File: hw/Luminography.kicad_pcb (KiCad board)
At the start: 2 copper layers, 100 x 100 mm, 112 parts, among them J1 USB_C_Receptacle_PowerOnly_6P, J2 Conn_01x04, Q1 2N7002, SW1 SW_Push, SW2 SW_Push, U1 LTC4054ES5-4.2, U10 MAX98357AETE+, U100 BH1750FVI-TR, U101 BH1750FVI-TR, U102 BH1750FVI-TR, U103 BH1750FVI-TR, U104 BH1750FVI-TR, U105 BH1750FVI-TR, U106 BH1750FVI-TR, U107 BH1750FVI-TR, U108 BH1750FVI-TR, U109 BH1750FVI-TR, U110 BH1750FVI-TR, U111 BH1750FVI-TR, U112 BH1750FVI-TR, U113 BH1750FVI-TR, U114 BH1750FVI-TR, U115 BH1750FVI-TR, U116 BH1750FVI-TR, U117 BH1750FVI-TR, U118 BH1750FVI-TR, U119 BH1750FVI-TR, U120 BH1750FVI-TR, U121 BH1750FVI-TR, U122 BH1750FVI-TR, U123 BH1750FVI-TR, U2 XS3A1T3157GMX, U3 SPX3819M5-L-3-3, U4 MAX17048G+T10, U5 STM32G030K6Tx, U6 ZJY128R-IG01, U7 W25Q16JVUXIQ, U8 BMI270, U9 MMC5603NJ, X1 12.288MHz

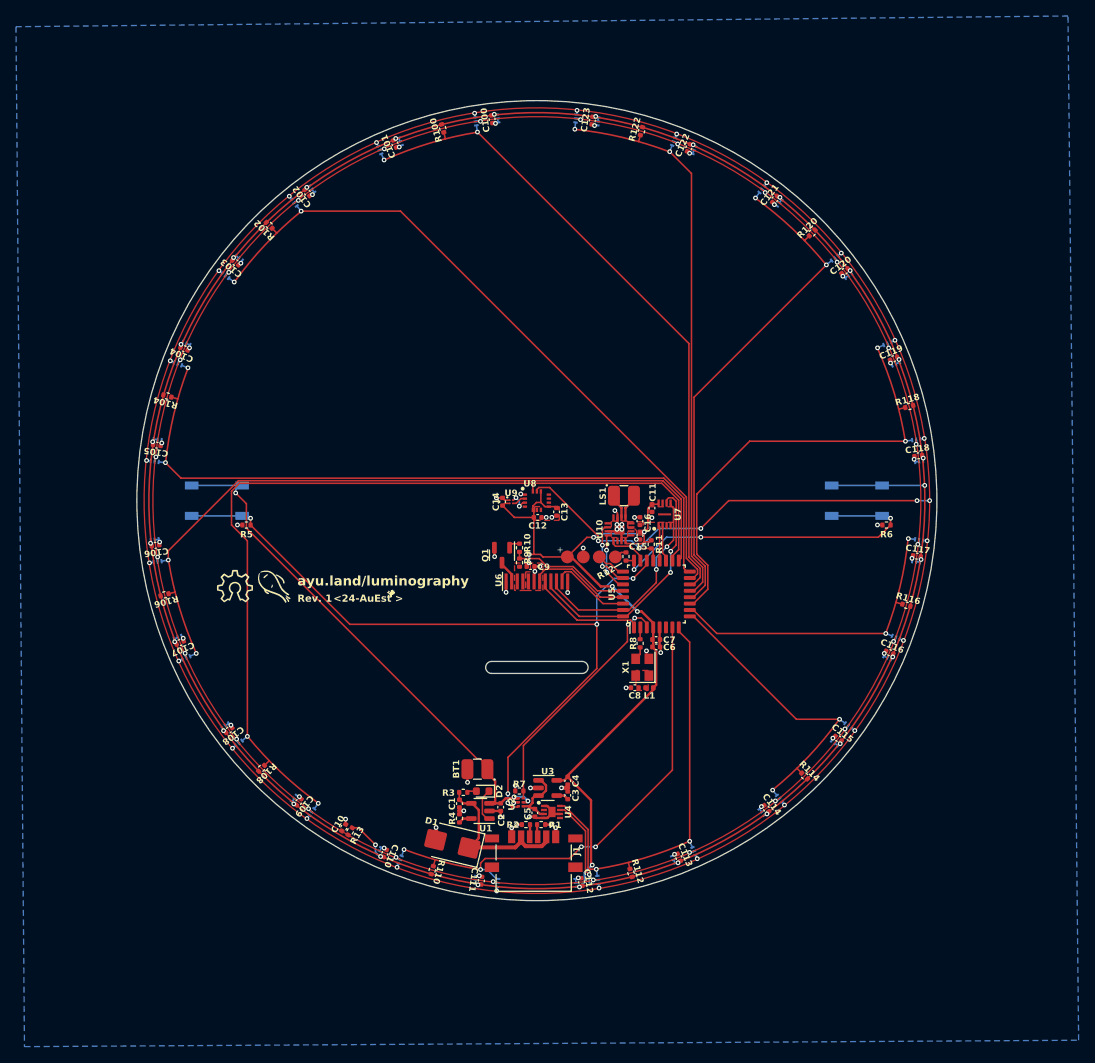
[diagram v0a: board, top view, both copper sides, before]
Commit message: 🚧 Add LEDs
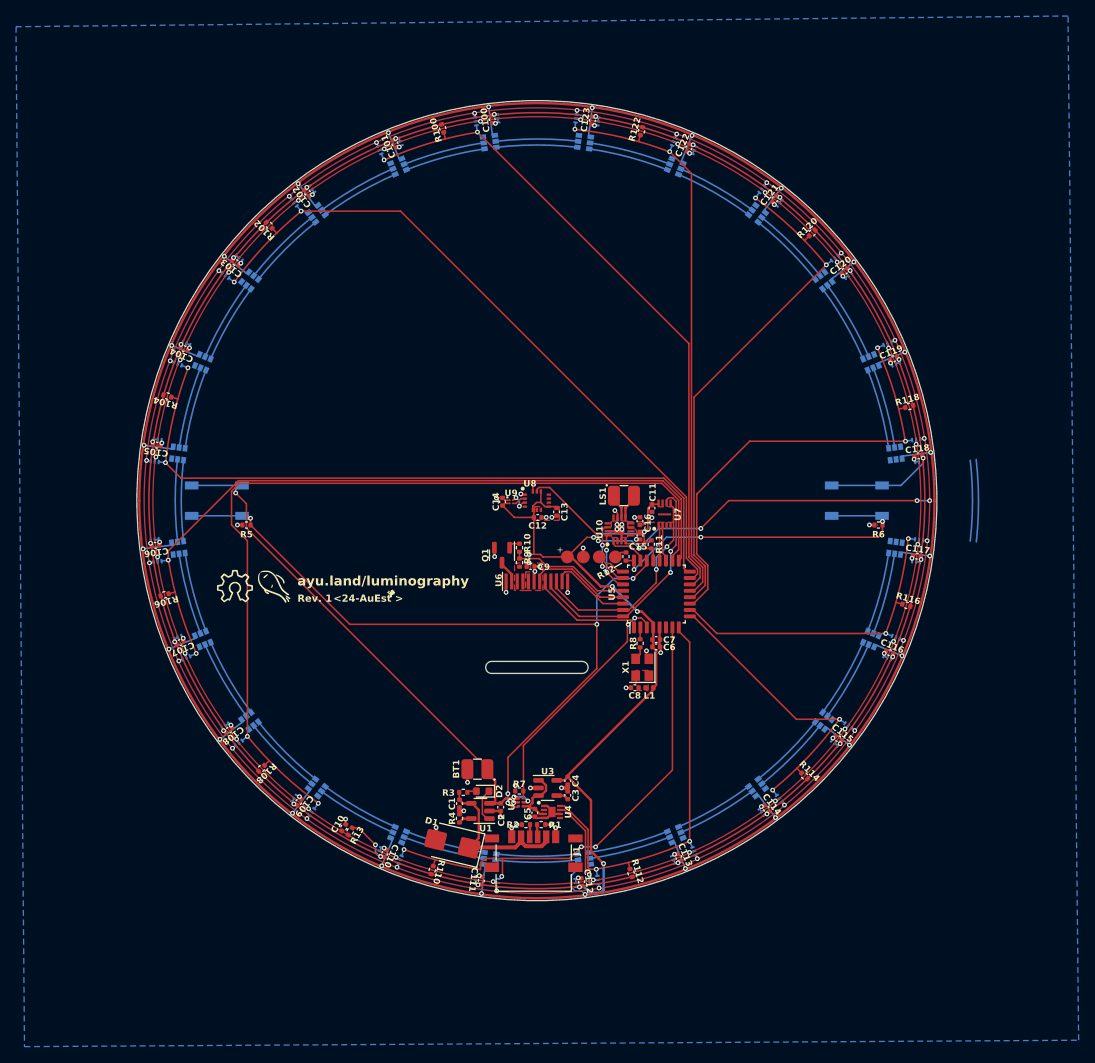
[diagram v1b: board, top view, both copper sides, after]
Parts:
- added U200: HD107S, Luminography_footprints:HD107S_2020_6, B.Cu at (94.1, 55.2)
- added U201: HD107S, Luminography_footprints:HD107S_2020_6, B.Cu at (82.7, 58.2)
- added U202: HD107S, Luminography_footprints:HD107S_2020_6, B.Cu at (72.5, 64.1)
- added U203: HD107S, Luminography_footprints:HD107S_2020_6, B.Cu at (64.1, 72.5)
- added U204: HD107S, Luminography_footprints:HD107S_2020_6, B.Cu at (58.2, 82.7)
- added U205: HD107S, Luminography_footprints:HD107S_2020_6, B.Cu at (55.2, 94.1)
- added U206: HD107S, Luminography_footprints:HD107S_2020_6, B.Cu at (55.2, 105.9)
- added U207: HD107S, Luminography_footprints:HD107S_2020_6, B.Cu at (58.2, 117.3)
- added U208: HD107S, Luminography_footprints:HD107S_2020_6, B.Cu at (64.1, 127.5)
- added U209: HD107S, Luminography_footprints:HD107S_2020_6, B.Cu at (72.5, 135.9)
- added U210: HD107S, Luminography_footprints:HD107S_2020_6, B.Cu at (82.7, 141.8)
- added U211: HD107S, Luminography_footprints:HD107S_2020_6, B.Cu at (94.1, 144.8)
- added U212: HD107S, Luminography_footprints:HD107S_2020_6, B.Cu at (105.9, 144.8)
- added U213: HD107S, Luminography_footprints:HD107S_2020_6, B.Cu at (117.3, 141.8)
- added U214: HD107S, Luminography_footprints:HD107S_2020_6, B.Cu at (127.5, 135.9)
- added U215: HD107S, Luminography_footprints:HD107S_2020_6, B.Cu at (135.9, 127.5)
- added U216: HD107S, Luminography_footprints:HD107S_2020_6, B.Cu at (141.8, 117.3)
- added U217: HD107S, Luminography_footprints:HD107S_2020_6, B.Cu at (144.8, 105.9)
- added U218: HD107S, Luminography_footprints:HD107S_2020_6, B.Cu at (144.8, 94.1)
- added U219: HD107S, Luminography_footprints:HD107S_2020_6, B.Cu at (141.8, 82.7)
- added U220: HD107S, Luminography_footprints:HD107S_2020_6, B.Cu at (135.9, 72.5)
- added U221: HD107S, Luminography_footprints:HD107S_2020_6, B.Cu at (127.5, 64.1)
- added U222: HD107S, Luminography_footprints:HD107S_2020_6, B.Cu at (117.3, 58.2)
- added U223: HD107S, Luminography_footprints:HD107S_2020_6, B.Cu at (105.9, 55.2)
- moved R6 1.00 mm to (142.7, 103.0)
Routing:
- net +5V: track 0.00 -> 370.2 mm, vias 0 -> 24
- net (no net): track 0.00 -> 20.5 mm
- net Net-(U207-CI): track 0.00 -> 10.3 mm
- net Net-(U201-CI): track 0.00 -> 10.3 mm
- net Net-(U216-CI): track 0.00 -> 10.3 mm
- net Net-(U215-CI): track 0.00 -> 10.3 mm
- net Net-(U209-CI): track 0.00 -> 10.3 mm
- net Net-(U204-CI): track 0.00 -> 10.3 mm
- net Net-(U200-CO): track 0.00 -> 10.3 mm
- net Net-(U202-CI): track 0.00 -> 10.3 mm
- net Net-(U222-CI): track 0.00 -> 10.3 mm
- net Net-(U219-CI): track 0.00 -> 10.3 mm
- net Net-(U213-CI): track 0.00 -> 10.3 mm
- net Net-(U221-CI): track 0.00 -> 10.3 mm
- net Net-(U206-CI): track 0.00 -> 10.3 mm
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
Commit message: 🚧 Finally, add LEDS (board revision WIP)
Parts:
- removed the C8 at (112.2, 123.4)
- removed the R12 at (111.1, 107.0)
- removed X1: 12.288MHz, Oscillator:Oscillator_SMD_Abracon_ASE-4Pin_3.2x2.5mm
- added C10: 100n, Capacitor_SMD:C_0402_1005Metric, F.Cu at (116.7, 117.8)
- added C11: 6.8p, Capacitor_SMD:C_0402_1005Metric, F.Cu at (113.0, 121.0)
- added C12: 6.8p, Capacitor_SMD:C_0402_1005Metric, F.Cu at (118.2, 120.7)
- added C14: 100n, Capacitor_SMD:C_0402_1005Metric, F.Cu at (127.5, 106.1)
- added C15: 100n, Capacitor_SMD:C_0402_1005Metric, F.Cu at (128.4, 112.6)
- added C5: 10u, Capacitor_SMD:C_0402_1005Metric, F.Cu at (102.9, 131.8)
- added C6: 10u, Capacitor_SMD:C_0402_1005Metric, F.Cu at (103.2, 127.9)
- added R14: 1M, Resistor_SMD:R_0402_1005Metric, F.Cu at (126.6, 112.6)
- added R9: 2.2k, Resistor_SMD:R_0402_1005Metric, F.Cu at (105.7, 129.3)
- added U4: TPS61220DCK, Package_TO_SOT_SMD:Texas_R-PDSO-G6, F.Cu at (103.4, 129.8)
- added U8: TXS0102DCT, Package_SO:SSOP-8_2.95x2.8mm_P0.65mm, F.Cu at (127.5, 109.4)
- added Y1: 32MHz 12pF, Crystal:Crystal_SMD_3225-4Pin_3.2x2.5mm, F.Cu at (115.6, 121.0)
- L1: value 10n -> 10u; footprint Inductor_SMD:L_0402_1005Metric -> Inductor_SMD:L_Sunlord_SWPA252012S
- R8: value 0 TBD -> 1.8M
- U6: renamed from U5; value STM32G030K6Tx -> STM32G030C8Tx; footprint Package_QFP:LQFP-32_7x7mm_P0.8mm -> Package_QFP:LQFP-48_7x7mm_P0.5mm
- moved L1 15.8 mm to (100.2, 130.9), turned to 90 degrees
- moved R8 13.0 mm to (106.7, 129.3), turned to -90 degrees
- moved C8 0.37 mm to (114.5, 118.3)
- moved C9 0.37 mm to (114.5, 117.4)
- renumbered C9 to C13, C10 to C16, C11 to C17, C12 to C18, C13 to C19, C14 to C20, C15 to C21, C16 to C22, C5 to C7, C6 to C8, C7 to C9, R9 to R10, R10 to R11, R11 to R12, U9 to U10, U8 to U11, U10 to U12, U4 to U5, U6 to U7, U7 to U9
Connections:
- L1 pad 1: VDD -> VRI
- R8 pad 1: Net-(X1-OUT) -> +5V
- R8 pad 2: Net-(U5-PC14) -> Net-(U4-FB)
- U217 pad 5: LED_CLK -> LED_CLK_5V
- U217 pad 6: LED_DATA -> LED_DATA_5V
- U6 pad 1: LCD_CS -> BTNA_INTR
- U6 pad 10: I2Cx_SDA_08 -> Net-(U6-NRST)
- U6 pad 11: I2Cx_SDA_09 -> I2Cx_SDA_05
- U6 pad 12: I2Cx_SDA_10 -> I2Cx_SDA_06
- U6 pad 13: I2Cx_SDA_11 -> I2Cx_SDA_07
- U6 pad 14: I2Cx_SDA_00 -> I2Cx_SDA_08
- U6 pad 15: I2Cx_SDA_01 -> LSH_OE
- U6 pad 16: I2Cx_SDA_02 -> LED_CLK
- U6 pad 17: I2Cx_SDA_03 -> BTNB_INTR
- U6 pad 18: I2Cx_SDA_04 -> LED_DATA
- U6 pad 19: SPI_MISO -> I2Cx_SDA_09
- U6 pad 2: Net-(U5-PC14) -> PWR_LATCH
- U6 pad 20: FLASH_CS -> I2Cx_SDA_10
- U6 pad 21: I2Cx_SCL -> I2Cx_SDA_11
- U6 pad 22: BTNA_INTR -> I2Cx_SDA_00
- U6 pad 23: I2S_SD -> I2Cx_SDA_01
- U6 pad 24: BTNB_INTR -> I2Cx_SDA_02
- U6 pad 25: SWCLK -> I2Cx_SDA_03
- U6 pad 26: I2S_WS -> I2Cx_SDA_04
- U6 pad 27: I2S_CK -> unconnected-(U6-PB15-Pad27)
- U6 pad 28: LCD_BL -> unconnected-(U6-PA8-Pad28)
- U6 pad 29: LCD_DC -> SPI_MISO
- U6 pad 3: PWR_LATCH -> unconnected-(U6-PC15-Pad3)
- U6 pad 30: LCD_RSTN -> FLASH_CS
- U6 pad 31: SPI_MOSI -> unconnected-(U6-PC7-Pad31)
- U6 pad 32: SPI_SCK -> I2Cx_SCL
- U6 pad 5: GND -> VDD
- U6 pad 6: unconnected-(U5-NRST-Pad6) -> VDD
- U6 pad 7: I2Cx_SDA_05 -> GND
- U6 pad 8: I2Cx_SDA_06 -> Net-(U6-PF0)
- U6 pad 9: I2Cx_SDA_07 -> Net-(U6-PF1)
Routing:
- net +5V: track 370.2 -> 404.5 mm, vias 24 -> 26
- net (no net): track 20.5 -> 0.00 mm
- net VDD: track 402.2 -> 420.5 mm, vias 32 -> 33
- net VRI: track 8.10 -> 18.9 mm
- net LSH_OE: track 0.00 -> 9.91 mm
- net LED_DATA: track 0.00 -> 9.55 mm
- net GND: track 48.1 -> 57.1 mm, vias 61 -> 68
- net LED_CLK: track 0.00 -> 8.86 mm
- net BTNB_INTR: track 43.5 -> 35.5 mm, vias 3 -> 1
- net Net-(U6-PF0): track 0.00 -> 8.06 mm
- net Net-(U6-PF1): track 0.00 -> 6.05 mm
- net BTNA_INTR: track 97.2 -> 93.4 mm, vias 5 -> 3
- net PWR_LATCH: track 30.6 -> 27.8 mm, vias 2 -> 0
- net Net-(U4-FB): track 0.00 -> 2.25 mm
- net I2Cx_SDA_04: track 112.3 -> 110.6 mm
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- added copper zone on F.Cu, net +5V
- added copper zone on F.Cu, net VRI
